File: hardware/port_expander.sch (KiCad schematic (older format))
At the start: 0 parts

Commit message: Stub port expander subcircuit
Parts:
- added U?: TCA9555, Housings_DFN_QFN:QFN-24-1EP_4x4mm_Pitch0.5mm, symbol TCA9555
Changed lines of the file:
@@
 $Descr A4 11693 8268
 encoding utf-8
-Sheet 2 22
+Sheet 22 22
 Title ""
 Date ""
@@
 Comment4 ""
 $EndDescr
+$Comp
+L TCA9555 U?
+U 1 1 54E9D22B
+P 5500 3750
+F 0 "U?" H 5500 2750 60  0000 C CNN
+F 1 "TCA9555" H 5500 4750 60  0000 C CNN
+F 2 "Housings_DFN_QFN:QFN-24-1EP_4x4mm_Pitch0.5mm" H 5500 3750 60  0001 C CNN
+F 3 "" H 5500 3750 60  0000 C CNN
+	1    5500 3750
+	1    0    0    -1
+$EndComp
 $EndSCHEMATC

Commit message: Specify QFN package in symbol name
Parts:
- U?: value TCA9555 -> TCA9555RTWR; symbol TCA9555 -> TCA9555RTWR
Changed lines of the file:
@@
 $EndDescr
 $Comp
-L TCA9555 U?
+L TCA9555RTWR U?
 U 1 1 54E9D22B
 P 5500 3750
 F 0 "U?" H 5500 2750 60  0000 C CNN
-F 1 "TCA9555" H 5500 4750 60  0000 C CNN
+F 1 "TCA9555RTWR" H 5500 4750 60  0000 C CNN
 F 2 "Housings_DFN_QFN:QFN-24-1EP_4x4mm_Pitch0.5mm" H 5500 3750 60  0001 C CNN
 F 3 "" H 5500 3750 60  0000 C CNN

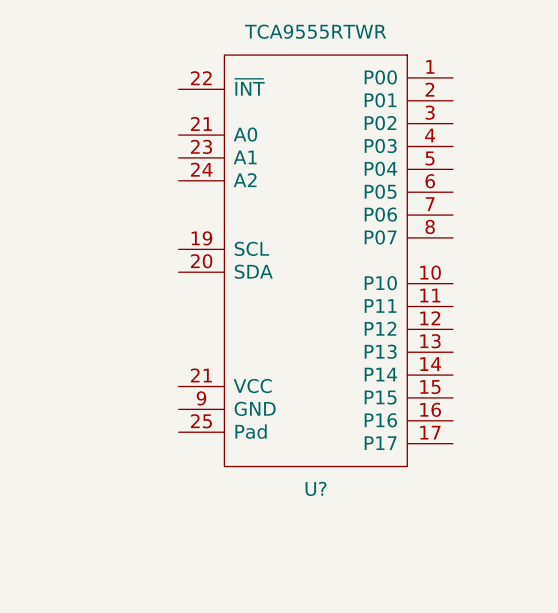
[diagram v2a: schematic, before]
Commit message: Draw port expander and integrate first instance
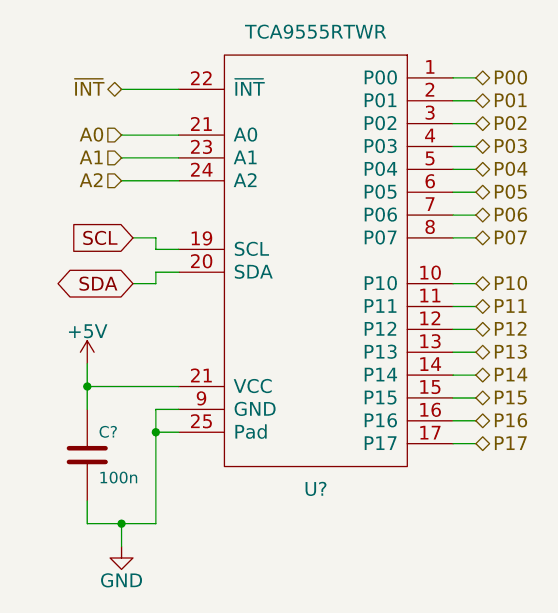
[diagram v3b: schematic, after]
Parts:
- added C?: 100n, symbol C
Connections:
- net P00: now reaches U?.1 (P00)
- net P10: now reaches U?.10 (P10)
- net P11: now reaches U?.11 (P11)
- net P12: now reaches U?.12 (P12)
- net P13: now reaches U?.13 (P13)
- net P14: now reaches U?.14 (P14)
- net P15: now reaches U?.15 (P15)
- net P16: now reaches U?.16 (P16)
- net P17: now reaches U?.17 (P17)
- net SCL: now reaches U?.19 (SCL)
- net P01: now reaches U?.2 (P01)
- net SDA: now reaches U?.20 (SDA)
- net A0: now reaches U?.21 (VCC)
- net ~INT: now reaches U?.22 (~INT)
- net A1: now reaches U?.23 (A1)
- net A2: now reaches U?.24 (A2)
- net GND: now reaches U?.25 (Pad)
- net GND: now also U?.9 (GND), C?.2
- net P02: now reaches U?.3 (P02)
- net P03: now reaches U?.4 (P03)
- net P04: now reaches U?.5 (P04)
- net P05: now reaches U?.6 (P05)
- net P06: now reaches U?.7 (P06)
- net P07: now reaches U?.8 (P07)
- new net +5V: C?.1, U?.21 (VCC)
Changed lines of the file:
@@
 	1    0    0    -1
 $EndComp
+Text GLabel 4700 3650 0    60   Input ~ 0
+SCL
+Text GLabel 4700 3850 0    60   BiDi ~ 0
+SDA
+Wire Wire Line
+	4700 3650 4800 3650
+Wire Wire Line
+	4800 3650 4800 3700
+Wire Wire Line
+	4800 3700 4900 3700
+Wire Wire Line
+	4700 3850 4800 3850
+Wire Wire Line
+	4800 3850 4800 3800
+Wire Wire Line
+	4800 3800 4900 3800
+Text HLabel 6200 2950 2    60   BiDi ~ 0
+P00
+Text HLabel 6200 3050 2    60   BiDi ~ 0
+P01
+Text HLabel 6200 3150 2    60   BiDi ~ 0
+P02
+Text HLabel 6200 3250 2    60   BiDi ~ 0
+P03
+Text HLabel 6200 3350 2    60   BiDi ~ 0
+P04
+Text HLabel 6200 3450 2    60   BiDi ~ 0
+P05
+Text HLabel 6200 3550 2    60   BiDi ~ 0
+P06
+Text HLabel 6200 3650 2    60   BiDi ~ 0
+P07
+Text HLabel 6200 3850 2    60   BiDi ~ 0
+P10
+Text HLabel 6200 3950 2    60   BiDi ~ 0
+P11
+Text HLabel 6200 4050 2    60   BiDi ~ 0
+P12
+Text HLabel 6200 4150 2    60   BiDi ~ 0
+P13
+Text HLabel 6200 4250 2    60   BiDi ~ 0
+P14
+Text HLabel 6200 4350 2    60   BiDi ~ 0
+P15
+Text HLabel 6200 4450 2    60   BiDi ~ 0
+P16
+Text HLabel 6200 4550 2    60   BiDi ~ 0
+P17
+Wire Wire Line
+	6100 2950 6200 2950
+Wire Wire Line
+	6100 3050 6200 3050
+Wire Wire Line
+	6100 3150 6200 3150
+Wire Wire Line
+	6100 3250 6200 3250
+Wire Wire Line
+	6100 3350 6200 3350
+Wire Wire Line
+	6100 3450 6200 3450
+Wire Wire Line
+	6100 3550 6200 3550
+Wire Wire Line
+	6100 3650 6200 3650
+Wire Wire Line
+	6100 3850 6200 3850
+Wire Wire Line
+	6100 3950 6200 3950
+Wire Wire Line
+	6100 4050 6200 4050
+Wire Wire Line
+	6100 4150 6200 4150
+Wire Wire Line
+	6100 4250 6200 4250
+Wire Wire Line
+	6100 4350 6200 4350
+Wire Wire Line
+	6100 4450 6200 4450
+Wire Wire Line
+	6100 4550 6200 4550
+$Comp
+L C C?
+U 1 1 54E9D730
+P 4500 4600
+F 0 "C?" H 4550 4700 50  0000 L CNN
+F 1 "100n" H 4550 4500 50  0000 L CNN
+F 2 "" H 4538 4450 30  0000 C CNN
+F 3 "" H 4500 4600 60  0000 C CNN
+	1    4500 4600
+	1    0    0    -1
+$EndComp
+Wire Wire Line
+	4900 4400 4800 4400
+Wire Wire Line
+	4800 4400 4800 4900
+Wire Wire Line
+	4500 4200 4500 4400
+Wire Wire Line
+	4500 4300 4900 4300
+Wire Wire Line
+	4900 4500 4800 4500
+Connection ~ 4800 4500
+Wire Wire Line
+	4800 4900 4500 4900
+Wire Wire Line
+	4500 4900 4500 4800
+$Comp
+L GND #PWR?
+U 1 1 54E9DA24
+P 4650 5000
+F 0 "#PWR?" H 4650 4750 60  0001 C CNN
+F 1 "GND" H 4650 4850 60  0000 C CNN
+F 2 "" H 4650 5000 60  0000 C CNN
+F 3 "" H 4650 5000 60  0000 C CNN
+	1    4650 5000
+	1    0    0    -1
+$EndComp
+Wire Wire Line
+	4650 5000 4650 4900
+Connection ~ 4650 4900
+Text HLabel 4650 3200 0    60   Input ~ 0
+A0
+Text HLabel 4650 3300 0    60   Input ~ 0
+A1
+Text HLabel 4650 3400 0    60   Input ~ 0
+A2
+Wire Wire Line
+	4650 3200 4900 3200
+Wire Wire Line
+	4900 3300 4650 3300
+Wire Wire Line
+	4650 3400 4900 3400
+Text HLabel 4650 3000 0    60   3State ~ 0
+~INT
+Wire Wire Line
+	4650 3000 4900 3000
+$Comp
+L +5V #PWR?
+U 1 1 54E9F047
+P 4500 4200
+F 0 "#PWR?" H 4500 4050 60  0001 C CNN
+F 1 "+5V" H 4500 4340 60  0000 C CNN
+F 2 "" H 4500 4200 60  0000 C CNN
+F 3 "" H 4500 4200 60  0000 C CNN
+	1    4500 4200
+	1    0    0    -1
+$EndComp
+Connection ~ 4500 4300
 $EndSCHEMATC
